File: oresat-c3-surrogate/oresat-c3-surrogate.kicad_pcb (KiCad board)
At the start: 2 copper layers, 99.8 x 94.6 mm, 38 parts, among them J1 J-SAMTEC-TFM-120-X1-XXX-D-RA, J2 Conn_01x04, J3 Terminal Block, J4 Barrel Jack, J5 Header, J6 Header, Q1 PMV45EN, Q2 DMP3050LVT-7, Q3 PMV45EN, Q4 DMP3050LVT-7, SW1 Slide Switch, SW2 Slide Switch, U1 Trinket-M0, U2 Seeed-USB-to-UART

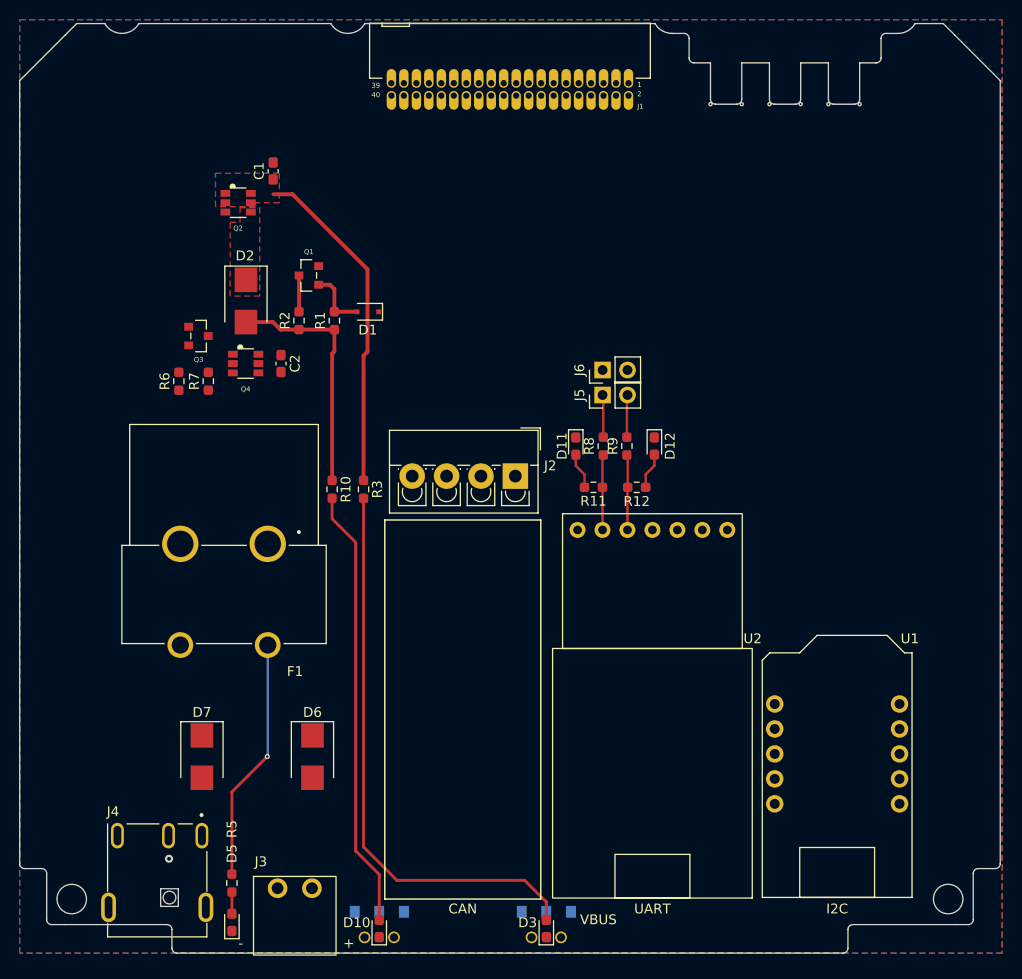
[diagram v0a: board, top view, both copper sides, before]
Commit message: Updated schematic and finished board layout
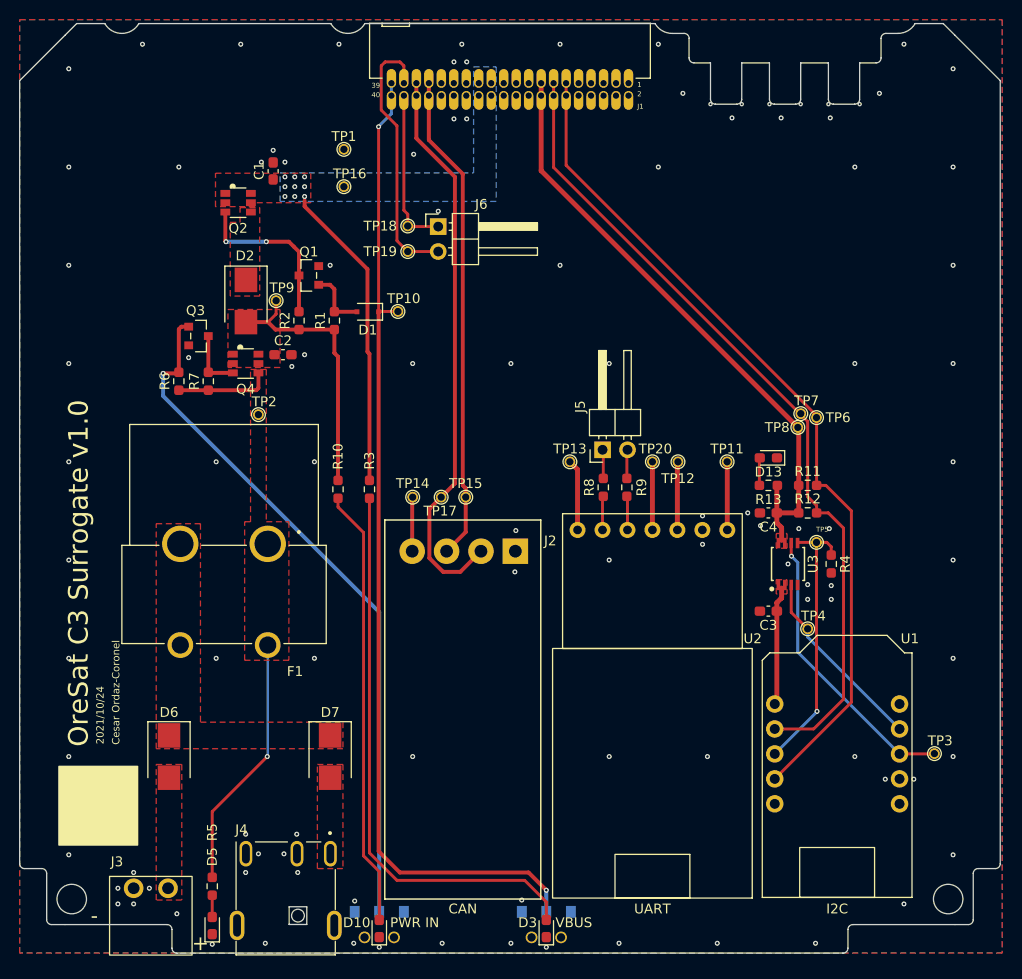
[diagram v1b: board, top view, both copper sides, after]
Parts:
- removed D11, D12: Green, LED_SMD:LED_0603_1608Metric_Pad1.05x0.95mm_HandSolder
- added C3: 1uF, Capacitor_SMD:C_0603_1608Metric_Pad1.08x0.95mm_HandSolder, F.Cu at (176.2, 115.2)
- added C4: 1uF, Capacitor_SMD:C_0603_1608Metric_Pad1.08x0.95mm_HandSolder, F.Cu at (176.2, 105.2)
- added D13: Green, LED_SMD:LED_0603_1608Metric_Pad1.05x0.95mm_HandSolder, F.Cu at (176.2, 99.6)
- added R13: 10k, Resistor_SMD:R_0603_1608Metric_Pad0.98x0.95mm_HandSolder, F.Cu at (176.2, 102.4)
- added R4: 23.7k, Resistor_SMD:R_0603_1608Metric_Pad0.98x0.95mm_HandSolder, F.Cu at (182.6, 110.4)
- added TP1: TEST-POINT-LARGE-SQUARE, oresat-misc:1X01, F.Cu at (133.0, 68.2)
- added TP10: TEST-POINT-LARGE-SQUARE, oresat-misc:1X01, F.Cu at (138.5, 84.7)
- added TP11: TEST-POINT-LARGE-SQUARE, oresat-misc:1X01, F.Cu at (172.0, 100.0)
- added TP12: TEST-POINT-LARGE-SQUARE, oresat-misc:1X01, F.Cu at (167.0, 100.0)
- added TP13: TEST-POINT-LARGE-SQUARE, oresat-misc:1X01, F.Cu at (156.0, 100.0)
- added TP14: TEST-POINT-LARGE-SQUARE, oresat-misc:1X01, F.Cu at (140.0, 103.6)
- added TP15: TEST-POINT-LARGE-SQUARE, oresat-misc:1X01, F.Cu at (145.4, 103.6)
- added TP16: TEST-POINT-LARGE-SQUARE, oresat-misc:1X01, F.Cu at (133.0, 72.0)
- added TP17: TEST-POINT-LARGE-SQUARE, oresat-misc:1X01, F.Cu at (142.9, 103.6)
- added TP18: TEST-POINT-LARGE-SQUARE, oresat-misc:1X01, F.Cu at (139.5, 76.0)
- added TP19: TEST-POINT-LARGE-SQUARE, oresat-misc:1X01, F.Cu at (139.5, 78.6)
- added TP2: TEST-POINT-LARGE-SQUARE, oresat-misc:1X01, F.Cu at (124.3, 95.2)
- added TP20: TEST-POINT-LARGE-SQUARE, oresat-misc:1X01, F.Cu at (164.4, 100.0)
- added TP3: TEST-POINT-LARGE-SQUARE, oresat-misc:1X01, F.Cu at (193.1, 129.7)
- added TP4: TEST-POINT-LARGE-SQUARE, oresat-misc:1X01, F.Cu at (180.2, 117.0)
- added TP5: TEST-POINT-LARGE-SQUARE, oresat-misc:1X01, F.Cu at (181.1, 108.2)
- added TP6: TEST-POINT-LARGE-SQUARE, oresat-misc:1X01, F.Cu at (181.1, 95.5)
- added TP7: TEST-POINT-LARGE-SQUARE, oresat-misc:1X01, F.Cu at (179.5, 95.1)
- added TP8: TEST-POINT-LARGE-SQUARE, oresat-misc:1X01, F.Cu at (179.2, 96.5)
- added TP9: TEST-POINT-LARGE-SQUARE, oresat-misc:1X01, F.Cu at (126.1, 83.6)
- added U3: MAX892LEUA+T, U-Maxim-MAX892LEUA+T-power-switch:MAX892LEUA+T, F.Cu at (178.2, 110.4)
- J5, J6: footprint Connector_PinHeader_2.54mm:PinHeader_1x02_P2.54mm_Vertical -> Connector_PinHeader_2.54mm:PinHeader_1x02_P2.54mm_Horizontal
- R11, R12: value 10k -> 4.7k
- moved J6 22.2 mm to (142.6, 76.1), turned to 0 degrees
- moved R11 21.8 mm to (180.2, 102.4)
- moved R12 17.6 mm to (180.2, 105.2), turned to 0 degrees
- moved J3 14.7 mm to (113.3, 143.4)
- moved D6 14.6 mm to (115.2, 130.0)
- moved J4 13.2 mm to (127.1, 144.4)
- moved D7 13.0 mm to (131.6, 130.0)
- moved J2 7.64 mm to (150.4, 109.1)
- moved J5 5.58 mm to (159.3, 98.8)
- moved R8 4.20 mm to (159.4, 102.6)
- moved R9 4.20 mm to (161.8, 102.6)
- moved D5 2.03 mm to (119.6, 147.2)
- moved R5 2.03 mm to (119.6, 143.2)
- moved C2 0.92 mm to (126.8, 89.1), turned to 0 degrees
- moved R10 0.60 mm to (132.4, 102.8)
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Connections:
- R11 pad 1: Net-(D11-Pad2) -> /OPD_PWR
- R11 pad 2: Net-(R8-Pad1) -> /OPD_SDA
- R12 pad 1: Net-(D12-Pad2) -> /OPD_PWR
- R12 pad 2: Net-(R9-Pad1) -> /OPD_SCL
- SW1 pad 1: Net-(Q3-Pad1) -> unconnected-(SW1-Pad1)
- SW2 pad 1: /~{SD} -> unconnected-(SW2-Pad1)
- U1 pad 3: unconnected-(U1-Pad3) -> /OPD_~{FAULT}
- U1 pad 4: unconnected-(U1-Pad4) -> /OPD_~{ENABLE}
- U1 pad 6: /OPD_PWR -> Net-(U3-Pad1)
- U1 pad 8: unconnected-(U1-Pad8) -> /OPD_ISET
- U2 pad 1: unconnected-(U2-Pad1) -> Net-(U2-Pad1)
- U2 pad 4: unconnected-(U2-Pad4) -> Net-(U2-Pad4)
- U2 pad 5: unconnected-(U2-Pad5) -> Net-(U2-Pad5)
- U2 pad 7: unconnected-(U2-Pad7) -> Net-(U2-Pad7)
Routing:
- net /~{SD}: track 0.00 -> 101.6 mm, vias 0 -> 2
- net /OPD_SDA: track 0.00 -> 86.6 mm
- net /OPD_SCL: track 0.00 -> 83.9 mm
- net Net-(Q3-Pad1): track 0.00 -> 71.1 mm, vias 0 -> 1
- net /OPD_PWR: track 0.00 -> 62.6 mm
- net /CAN1_L: track 0.00 -> 57.7 mm
- net /CAN1_H: track 0.00 -> 50.0 mm
- net /OPD_~{FAULT}: track 0.00 -> 29.6 mm, vias 0 -> 1
- net /OPD_ISET: track 0.00 -> 28.1 mm, vias 0 -> 1
- net /C3-UART-TX: track 0.00 -> 27.5 mm
- net /OPD_~{ENABLE}: track 0.00 -> 19.2 mm
- net /C3-UART-RX: track 0.00 -> 16.6 mm
- net Net-(Q1-Pad3): track 3.69 -> 17.0 mm, vias 0 -> 2
- net Net-(U3-Pad1): track 0.00 -> 12.1 mm
- net Net-(F1-Pad1_1): track 24.8 -> 35.7 mm
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- added copper zone on F.Cu, net /OPD_PWR
- added copper zone on F.Cu, net Net-(C2-Pad1)
- added copper zone on F.Cu, net Net-(D6-Pad1)
- added copper zone on F.Cu, net Net-(D6-Pad2)
- added copper zone on F.Cu, net Net-(D7-Pad2)
- added copper zone on F.Cu, net Net-(F1-Pad1_1)
- added copper zone on F.Cu, net Net-(U3-Pad1)
- added copper zone on B.Cu, net VBUS
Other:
- board text added: "2021/10/24"
- board text added: "Cesar Ordaz-Coronel"
- board text added: "OreSat C3 Surrogate v1.0"
- board text added: "PWR IN"

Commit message: Updated surrogate board. Moved D2 on schematic, fixed UART pin headers, rotated fuse holder.
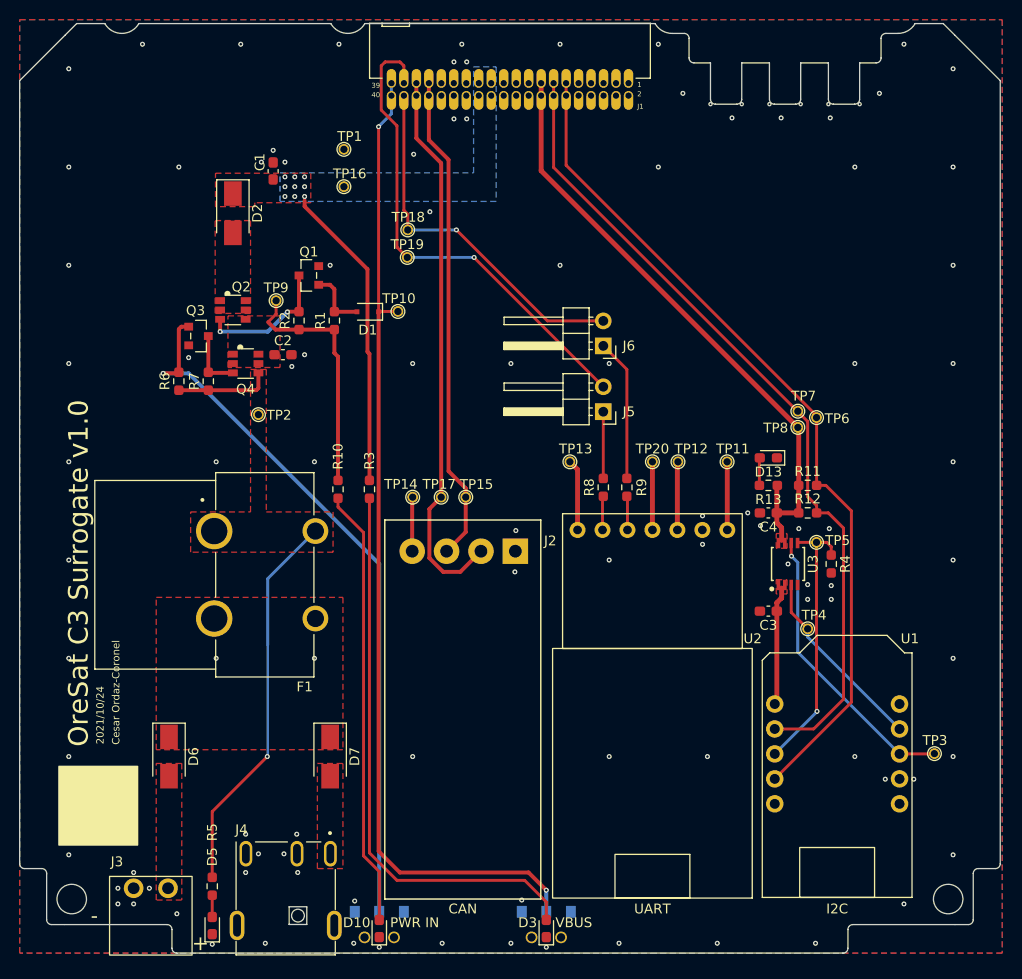
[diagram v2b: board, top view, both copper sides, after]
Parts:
- D2, D6, D7: footprint Diode_SMD:D_SMB -> Diode_SMD:D_SMA
- moved J6 20.7 mm to (159.4, 88.2), turned to 180 degrees
- moved Q2 10.9 mm to (121.7, 84.5)
- moved D2 9.03 mm to (121.7, 74.7)
- moved F1 4.61 mm to (125.0, 111.5), turned to -90 degrees
- moved J5 3.88 mm to (159.4, 94.9), turned to 180 degrees
- moved TP19 0.60 mm to (139.4, 79.2)
- moved TP18 0.40 mm to (139.5, 76.4)
- moved TP7 0.39 mm to (179.2, 94.8)
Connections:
- net /CAN1_H renamed CAN1_H
- net /CAN1_L renamed CAN1_L
- net /OPD_PWR renamed OPD_PWR
- net /OPD_SCL renamed OPD_SCL
- net /OPD_SDA renamed OPD_SDA
- D2 pad 1: Net-(D2-Pad1) -> VBUS
- D2 pad 2: Net-(C2-Pad1) -> Net-(D2-Pad2)
- J1 pad 37: /C3-UART-TX -> C3-UART-TX
- J1 pad 38: /C3-UART-RX -> C3-UART-RX
- J5 pad 2: Net-(J5-Pad2) -> C3-UART-TX
- J6 pad 1: /C3-UART-RX -> Net-(R9-Pad2)
- J6 pad 2: /C3-UART-TX -> C3-UART-RX
- Q2 pad 1: VBUS -> Net-(D2-Pad2)
- Q2 pad 2: VBUS -> Net-(D2-Pad2)
- Q2 pad 4: Net-(D2-Pad1) -> Net-(C2-Pad1)
- Q2 pad 5: VBUS -> Net-(D2-Pad2)
- Q2 pad 6: VBUS -> Net-(D2-Pad2)
- R9 pad 2: Net-(J5-Pad2) -> Net-(R9-Pad2)
- TP18 pad 1: /C3-UART-RX -> C3-UART-RX
- TP19 pad 1: /C3-UART-TX -> C3-UART-TX
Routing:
- net C3-UART-TX: track 0.00 -> 50.4 mm, vias 0 -> 1
- net C3-UART-RX: track 0.00 -> 37.6 mm, vias 0 -> 1
- net /C3-UART-TX: track 27.5 -> 0.00 mm
- net /C3-UART-RX: track 16.6 -> 0.00 mm
- net Net-(R9-Pad2): track 0.00 -> 14.5 mm
- net Net-(F1-Pad1_1): track 35.7 -> 49.3 mm
- net Net-(R8-Pad2): track 2.94 -> 6.79 mm
- net Net-(Q1-Pad3): track 17.0 -> 13.8 mm
- net Net-(J5-Pad2): track 2.94 -> 0.00 mm
- net Net-(C2-Pad1): track 27.3 -> 25.1 mm
- net Net-(Q3-Pad1): track 71.1 -> 72.6 mm
- net CAN1_L: track 57.7 -> 56.6 mm
- added copper zone on F.Cu, net Net-(D2-Pad2)
- removed copper zone on F.Cu, net Net-(D2-Pad1)
